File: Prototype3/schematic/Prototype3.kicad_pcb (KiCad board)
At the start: 2 copper layers, 95 x 72 mm, 28 parts, among them J1 Conn_I2C_Master, J2 Conn_Micro_SD, J3 Conn_USB_Serial, U1 ATmega1284P-PU, U2 HM628128DLP-5, U3 HD63C09E, U4 ATmega328-PU, Y1 20MHz, Y2 20MHz

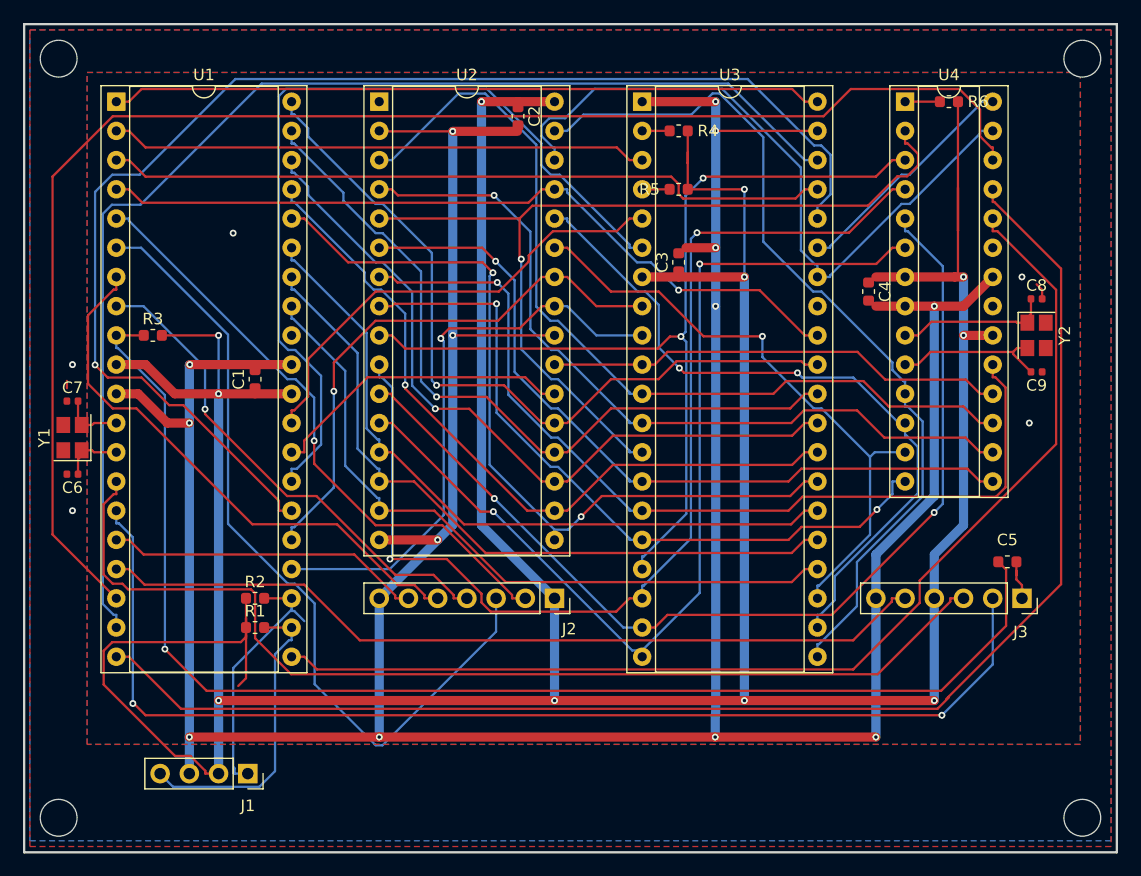
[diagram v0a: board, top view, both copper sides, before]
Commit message: Use 0.35mm for fill clearance
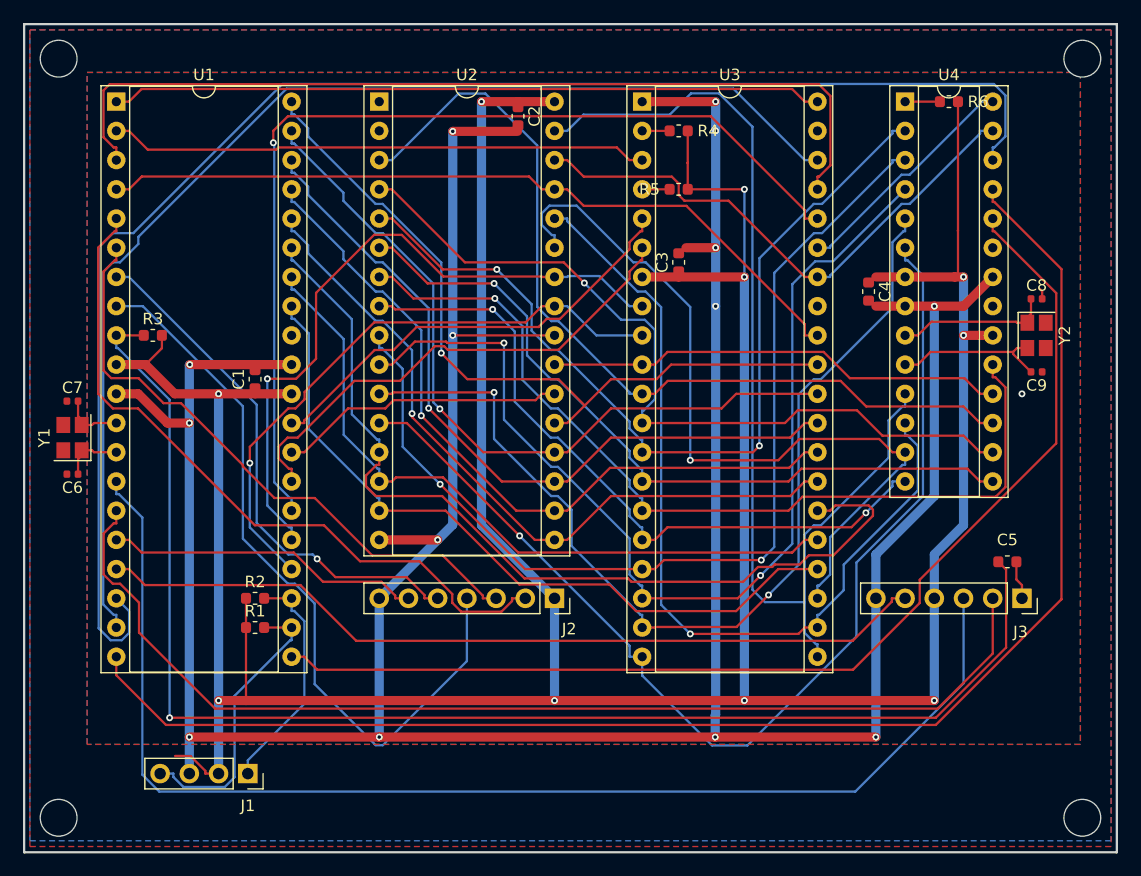
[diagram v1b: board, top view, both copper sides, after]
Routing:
- net VCC: track 355.2 -> 318.7 mm, vias 11 -> 10
- net /BA: track 75.6 -> 43.7 mm
- net /AVMA: track 114.7 -> 85.7 mm
- net /SD_SCK: track 43.5 -> 65.6 mm, vias 1 -> 0
- net /D5: track 62.3 -> 80.3 mm
- net /SD_DI: track 71.7 -> 53.8 mm
- net /DBG_RX: track 92.2 -> 109.9 mm
- net GND: track 320.5 -> 304.2 mm, vias 19 -> 15
- net /A15: track 53.5 -> 69.7 mm
- net /A13: track 76.5 -> 92.5 mm
- net /~RESET: track 63.2 -> 79.2 mm
- net /A14: track 62.4 -> 75.4 mm, vias 2 -> 1
- net /CLK_E: track 61.2 -> 48.4 mm
- net /A0: track 48.0 -> 58.8 mm
- net /A12: track 85.7 -> 95.5 mm, vias 2 -> 1
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
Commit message: Add keepout zones around connector and board edges
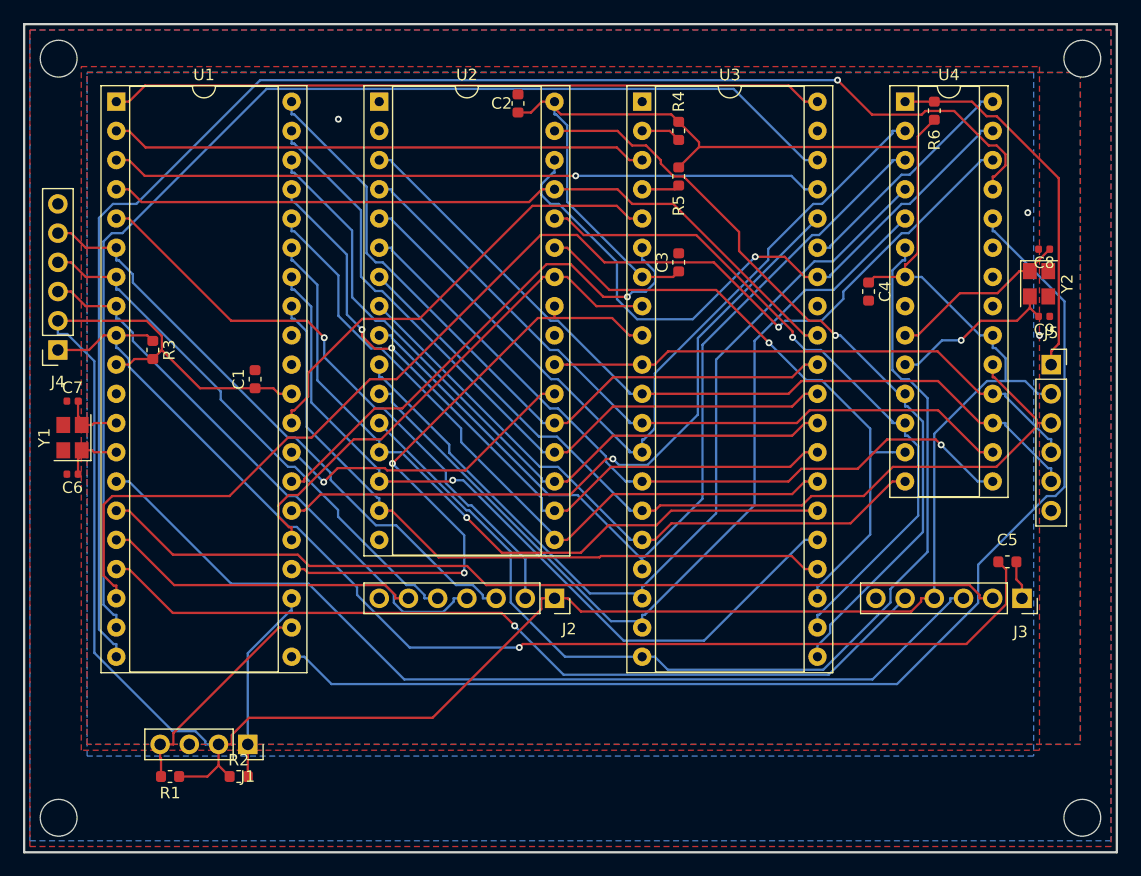
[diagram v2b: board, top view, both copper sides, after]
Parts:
- added J4: Conn_AVR_ISP, Connector_PinSocket_2.54mm:PinSocket_1x06_P2.54mm_Vertical, F.Cu at (103.9, 98.3)
- added J5: Conn_AVR_ISP, Connector_PinSocket_2.54mm:PinSocket_1x06_P2.54mm_Vertical, F.Cu at (190.3, 99.6)
- moved R2 15.6 mm to (119.7, 135.4)
- moved R1 14.9 mm to (113.7, 135.4), turned to 180 degrees
- moved C9 4.87 mm to (189.7, 95.4)
- moved Y2 4.49 mm to (189.2, 92.6)
- moved C8 4.37 mm to (189.7, 89.6), turned to 180 degrees
- moved J1 2.54 mm to (120.4, 132.6)
- moved R6 1.49 mm to (180.1, 77.5), turned to 90 degrees
- moved R3 1.27 mm to (112.2, 98.3), turned to 270 degrees
- moved C2 1.12 mm to (143.9, 76.9), turned to 90 degrees
- moved R5 1.12 mm to (157.9, 83.2), turned to 90 degrees
- turned R4 to 90 degrees
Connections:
- net /~DBG_RST renamed /~DBG_RST~
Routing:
- net GND: track 304.2 -> 0.00 mm, vias 15 -> 3
- net VCC: track 318.7 -> 271.0 mm, vias 10 -> 0
- net Net-(J5-Pad1): track 3.02 -> 32.6 mm
- net /DBG_RX: track 109.9 -> 83.9 mm
- net /~INT: track 131.2 -> 105.5 mm, vias 0 -> 1
- net /AVMA: track 85.7 -> 60.6 mm
- net /A13: track 92.5 -> 68.8 mm, vias 0 -> 1
- net /~RESET: track 79.2 -> 62.0 mm, vias 0 -> 1
- net /DBG_TX: track 96.6 -> 79.5 mm
- net /SD_SCK: track 65.6 -> 49.3 mm
- net /~DBG_RST~: track 120.6 -> 104.5 mm
- net /A15: track 69.7 -> 53.7 mm
- net /D5: track 80.3 -> 64.4 mm, vias 0 -> 1
- net /A14: track 75.4 -> 60.3 mm
- net /A0: track 58.8 -> 44.6 mm, vias 1 -> 0
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
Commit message: Swap ~INT~ and ~DBG_RTS~
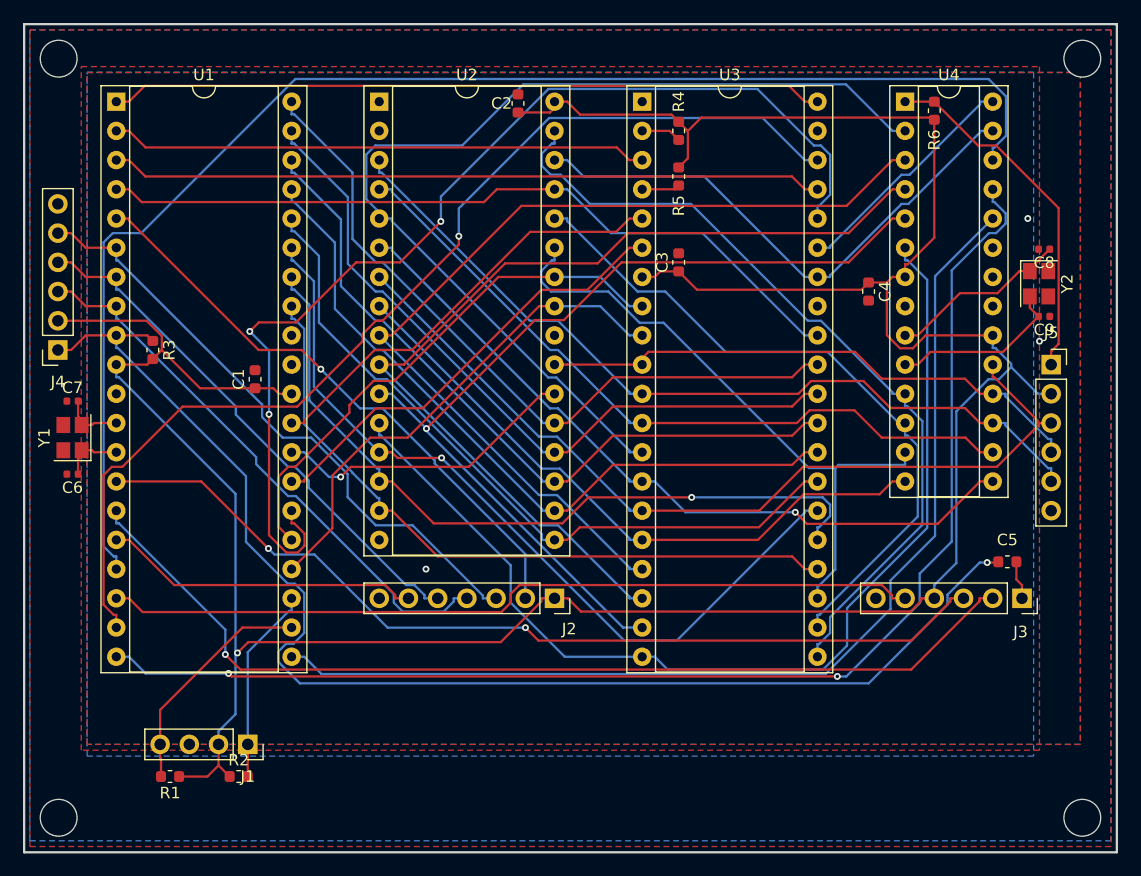
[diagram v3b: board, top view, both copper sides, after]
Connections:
- U1 pad 17: /~DBG_RTS -> /~INT
- U1 pad 18: /~INT -> /~DBG_RTS
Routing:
- net /AVMA: track 60.6 -> 94.9 mm, vias 1 -> 3
- net /A5: track 70.0 -> 88.8 mm
- net /~ACK: track 129.2 -> 113.2 mm, vias 1 -> 2
- net /~INT: track 105.5 -> 120.1 mm, vias 1 -> 0
- net /A1: track 55.9 -> 43.7 mm, vias 2 -> 0
- net /LIC: track 104.3 -> 92.5 mm, vias 0 -> 1
- net /~STEP: track 103.2 -> 92.7 mm
- net /CLK_E: track 57.6 -> 47.7 mm, vias 1 -> 0
- net /~DBG_RST~: track 104.5 -> 114.1 mm
- net /DBG_TX: track 79.5 -> 86.5 mm, vias 0 -> 1
- net VCC: track 271.0 -> 264.6 mm, vias 0 -> 1
- net /D5: track 64.4 -> 70.7 mm
- net /A9: track 77.2 -> 83.4 mm
- net /BA: track 44.8 -> 39.0 mm, vias 1 -> 0
- net /A10: track 78.2 -> 83.4 mm
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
